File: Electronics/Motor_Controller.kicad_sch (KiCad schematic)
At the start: 1 part, among them U1 RP2040

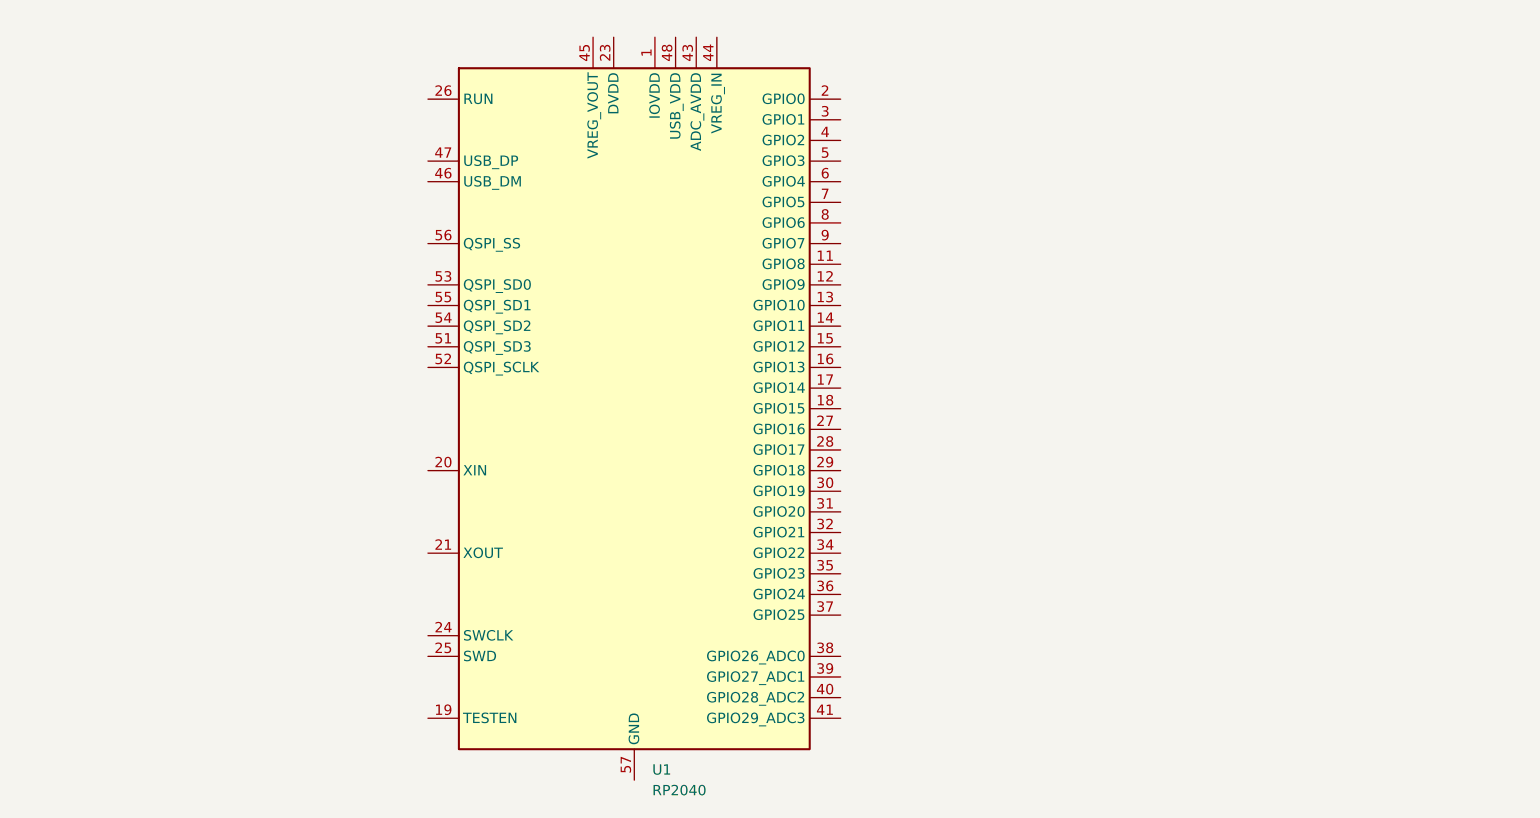
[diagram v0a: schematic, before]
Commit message: components for motor controller
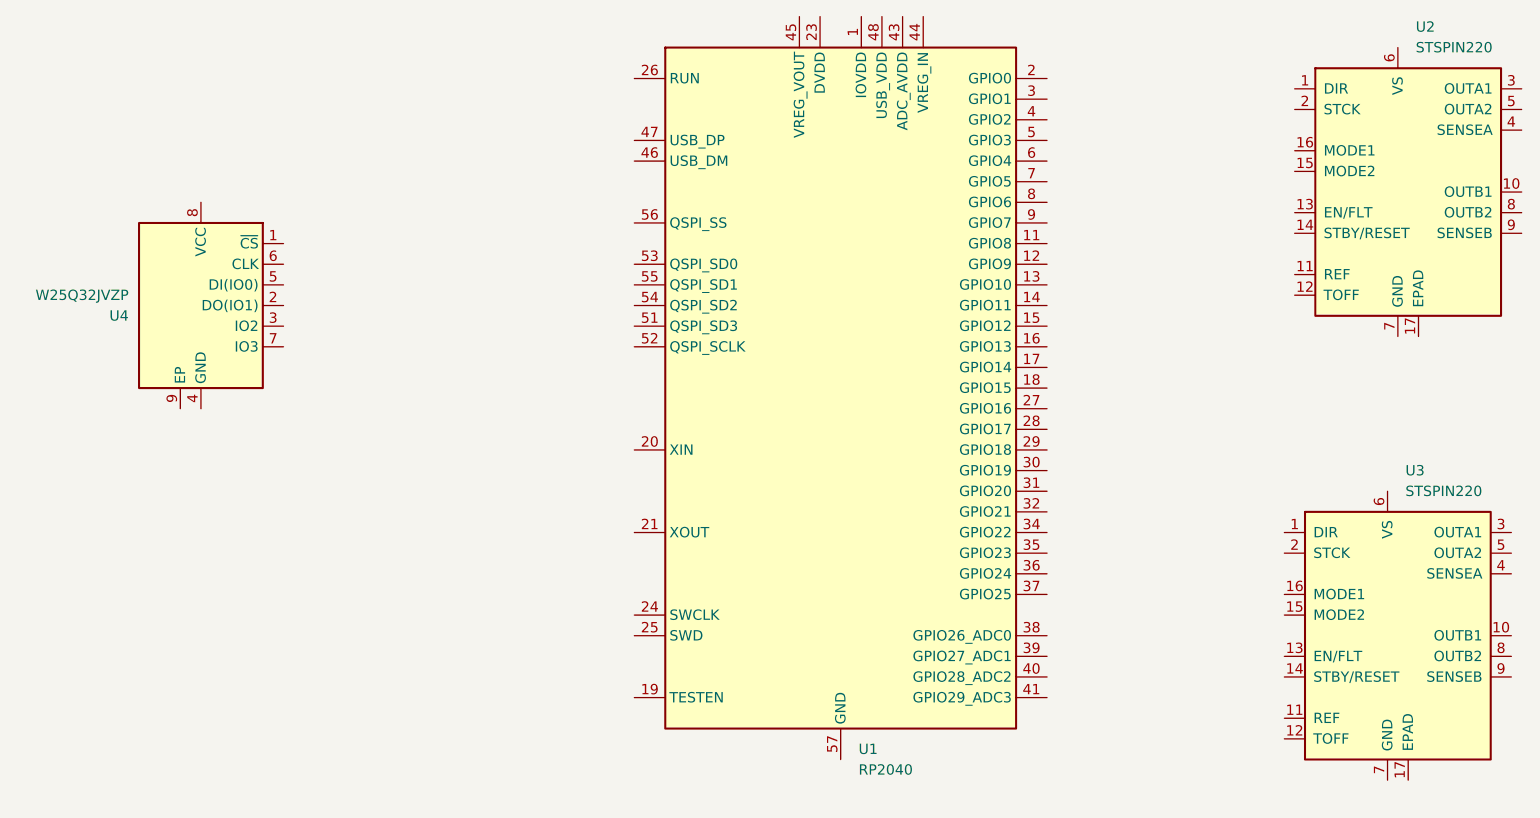
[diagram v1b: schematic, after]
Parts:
- added U2, U3: STSPIN220, Package_DFN_QFN:VQFN-16-1EP_3x3mm_P0.5mm_EP1.8x1.8mm, symbol Driver_Motor:STSPIN220
- added U4: W25Q32JVZP, Package_SON:WSON-8-1EP_6x5mm_P1.27mm_EP3.4x4.3mm, symbol Memory_Flash:W25Q32JVZP
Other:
- moved on the sheet: U1
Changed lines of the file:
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@@
 (kicad_sch (version 20230121) (generator eeschema)
   (paper "A4")
-  (symbol (lib_id "MCU_RaspberryPi:RP2040") (at 91.44 83.82 0) (unit 1)
+  (symbol (lib_id "Driver_Motor:STSPIN220") (at 184.15 111.76 0) (unit 1)
     (in_bom yes) (on_board yes) (dnp no) (fields_autoplaced)
-    (property "Reference" "U1" (at 93.6341 128.27 0)
+    (property "Reference" "U3" (at 186.3441 91.44 0)
       (effects (font (size 1.27 1.27)) (justify left))
     )
-    (property "Value" "RP2040" (at 93.6341 130.81 0)
+    (property "Value" "STSPIN220" (at 186.3441 93.98 0)
       (effects (font (size 1.27 1.27)) (justify left))
     )
-    (property "Footprint" "Package_DFN_QFN:QFN-56-1EP_7x7mm_P0.4mm_EP3.2x3.2mm" (at 91.44 83.82 0)
+    (property "Footprint" "Package_DFN_QFN:VQFN-16-1EP_3x3mm_P0.5mm_EP1.8x1.8mm" (at 189.23 92.71 0)
+      (effects (font (size 1.27 1.27)) (justify left) hide)
+    )
+    (property "Datasheet" "www.st.com/resource/en/datasheet/stspin220.pdf" (at 187.96 105.41 0)
       (effects (font (size 1.27 1.27)) hide)
     )
-    (property "Datasheet" "https://datasheets.raspberrypi.com/rp2040/rp2040-datasheet.pdf" (at 91.44 83.82 0)
+    (pin "5")
+    (pin "6")
+    (pin "13")
+    (pin "11")
+    (pin "14")
+    (pin "12")
+    (pin "15")
+    (pin "10")
+    (pin "16")
+    (pin "9")
+    (pin "1")
+    (pin "7")
+    (pin "3")
+    (pin "2")
+    (pin "8")
+    (pin "4")
+    (pin "17")
+    (instances
+      (project "Electronics"
+        (path "/4c70cac4-2e87-4919-a1c8-fe5f41acf493/95aef9fc-3811-4af8-99a5-cda59dbef7fc"
+          (reference "U3") (unit 1)
+        )
+      )
+    )
+  )
+  (symbol (lib_id "MCU_RaspberryPi:RP2040") (at 116.84 81.28 0) (unit 1)
+    (in_bom yes) (on_board yes) (dnp no) (fields_autoplaced)
+    (property "Reference" "U1" (at 119.0341 125.73 0)
+      (effects (font (size 1.27 1.27)) (justify left))
+    )
+    (property "Value" "RP2040" (at 119.0341 128.27 0)
+      (effects (font (size 1.27 1.27)) (justify left))
+    )
+    (property "Footprint" "Package_DFN_QFN:QFN-56-1EP_7x7mm_P0.4mm_EP3.2x3.2mm" (at 116.84 81.28 0)
+      (effects (font (size 1.27 1.27)) hide)
+    )
+    (property "Datasheet" "https://datasheets.raspberrypi.com/rp2040/rp2040-datasheet.pdf" (at 116.84 81.28 0)
       (effects (font (size 1.27 1.27)) hide)
     )
@@
         )
       )
+    )
+  )
+  (symbol (lib_id "Driver_Motor:STSPIN220") (at 185.42 57.15 0) (unit 1)
+    (in_bom yes) (on_board yes) (dnp no) (fields_autoplaced)
+    (property "Reference" "U2" (at 187.6141 36.83 0)
+      (effects (font (size 1.27 1.27)) (justify left))
+    )
+    (property "Value" "STSPIN220" (at 187.6141 39.37 0)
+      (effects (font (size 1.27 1.27)) (justify left))
+    )
+    (property "Footprint" "Package_DFN_QFN:VQFN-16-1EP_3x3mm_P0.5mm_EP1.8x1.8mm" (at 190.5 38.1 0)
+      (effects (font (size 1.27 1.27)) (justify left) hide)
+    )
+    (property "Datasheet" "www.st.com/resource/en/datasheet/stspin220.pdf" (at 189.23 50.8 0)
+      (effects (font (size 1.27 1.27)) hide)
+    )
+    (pin "5")
+    (pin "6")
+    (pin "13")
+    (pin "11")
+    (pin "14")
+    (pin "12")
+    (pin "15")
+    (pin "10")
+    (pin "16")
+    (pin "9")
+    (pin "1")
+    (pin "7")
+    (pin "3")
+    (pin "2")
+    (pin "8")
+    (pin "4")
+    (pin "17")
+    (instances
+      (project "Electronics"
+        (path "/4c70cac4-2e87-4919-a1c8-fe5f41acf493/95aef9fc-3811-4af8-99a5-cda59dbef7fc"
+          (reference "U2") (unit 1)
+        )
+      )
+    )
+  )
+  (symbol (lib_id "Memory_Flash:W25Q32JVZP") (at 38.1 71.12 0) (mirror y) (unit 1)
+    (in_bom yes) (on_board yes) (dnp no)
+    (property "Reference" "U4" (at 29.21 72.39 0)
+      (effects (font (size 1.27 1.27)) (justify left))
+    )
+    (property "Value" "W25Q32JVZP" (at 29.21 69.85 0)
+      (effects (font (size 1.27 1.27)) (justify left))
+    )
+    (property "Footprint" "Package_SON:WSON-8-1EP_6x5mm_P1.27mm_EP3.4x4.3mm" (at 38.1 71.12 0)
+      (effects (font (size 1.27 1.27)) hide)
+    )
+    (property "Datasheet" "http://www.winbond.com/resource-files/w25q32jv%20revg%2003272018%20plus.pdf" (at 38.1 73.66 0)
+      (effects (font (size 1.27 1.27)) hide)
+    )
+    (pin "9")
+    (pin "8")
+    (pin "3")
+    (pin "1")
+    (pin "6")
+    (pin "2")
+    (pin "7")
+    (pin "4")
+    (pin "5")
+    (instances
+      (project "Electronics"
+        (path "/4c70cac4-2e87-4919-a1c8-fe5f41acf493/95aef9fc-3811-4af8-99a5-cda59dbef7fc"
+          (reference "U4") (unit 1)
+        )
+      )

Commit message: symbol library
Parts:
- removed U2, U3: STSPIN220, Package_DFN_QFN:VQFN-16-1EP_3x3mm_P0.5mm_EP1.8x1.8mm, symbol Driver_Motor:STSPIN220
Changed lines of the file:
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@@
 (kicad_sch (version 20230121) (generator eeschema)
   (paper "A4")
-  (symbol (lib_id "Driver_Motor:STSPIN220") (at 184.15 111.76 0) (unit 1)
-    (in_bom yes) (on_board yes) (dnp no) (fields_autoplaced)
-    (property "Reference" "U3" (at 186.3441 91.44 0)
-      (effects (font (size 1.27 1.27)) (justify left))
-    )
-    (property "Value" "STSPIN220" (at 186.3441 93.98 0)
-      (effects (font (size 1.27 1.27)) (justify left))
-    )
-    (property "Footprint" "Package_DFN_QFN:VQFN-16-1EP_3x3mm_P0.5mm_EP1.8x1.8mm" (at 189.23 92.71 0)
-      (effects (font (size 1.27 1.27)) (justify left) hide)
-    )
-    (property "Datasheet" "www.st.com/resource/en/datasheet/stspin220.pdf" (at 187.96 105.41 0)
-      (effects (font (size 1.27 1.27)) hide)
-    )
-    (pin "5")
-    (pin "6")
-    (pin "13")
-    (pin "11")
-    (pin "14")
-    (pin "12")
-    (pin "15")
-    (pin "10")
-    (pin "16")
-    (pin "9")
-    (pin "1")
-    (pin "7")
-    (pin "3")
-    (pin "2")
-    (pin "8")
-    (pin "4")
-    (pin "17")
-    (instances
-      (project "Electronics"
-        (path "/4c70cac4-2e87-4919-a1c8-fe5f41acf493/95aef9fc-3811-4af8-99a5-cda59dbef7fc"
-          (reference "U3") (unit 1)
-        )
-      )
-    )
-  )
   (symbol (lib_id "MCU_RaspberryPi:RP2040") (at 116.84 81.28 0) (unit 1)
     (in_bom yes) (on_board yes) (dnp no) (fields_autoplaced)
@@
         )
       )
-    )
-  )
-  (symbol (lib_id "Driver_Motor:STSPIN220") (at 185.42 57.15 0) (unit 1)
-    (in_bom yes) (on_board yes) (dnp no) (fields_autoplaced)
-    (property "Reference" "U2" (at 187.6141 36.83 0)
-      (effects (font (size 1.27 1.27)) (justify left))
-    )
-    (property "Value" "STSPIN220" (at 187.6141 39.37 0)
-      (effects (font (size 1.27 1.27)) (justify left))
-    )
-    (property "Footprint" "Package_DFN_QFN:VQFN-16-1EP_3x3mm_P0.5mm_EP1.8x1.8mm" (at 190.5 38.1 0)
-      (effects (font (size 1.27 1.27)) (justify left) hide)
-    )
-    (property "Datasheet" "www.st.com/resource/en/datasheet/stspin220.pdf" (at 189.23 50.8 0)
-      (effects (font (size 1.27 1.27)) hide)
-    )
-    (pin "5")
-    (pin "6")
-    (pin "13")
-    (pin "11")
-    (pin "14")
-    (pin "12")
-    (pin "15")
-    (pin "10")
-    (pin "16")
-    (pin "9")
-    (pin "1")
-    (pin "7")
-    (pin "3")
-    (pin "2")
-    (pin "8")
-    (pin "4")
-    (pin "17")
-    (instances
-      (project "Electronics"
-        (path "/4c70cac4-2e87-4919-a1c8-fe5f41acf493/95aef9fc-3811-4af8-99a5-cda59dbef7fc"
-          (reference "U2") (unit 1)
-        )
-      )

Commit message: TMC2209 FOOTPRINT + SCHEMATIC
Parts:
- added C1: 100nF, symbol Device:C
- added U2: ~, Package_DFN_QFN:QFN-28-1EP_5x5mm_P0.5mm_EP3.75x3.75mm, symbol TMC2209-LA-T:TMC2209-LA-T
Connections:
- new net: C1.2, U2.6 (VCP)
- new net GND: U2.18 (GND), U2.3 (GND)
- new net VBAT: C1.1, U2.22 (VS), U2.28 (VS)
- new net VCC: U2.15 (VCC_IO), U2.17 (VREF)
- no-connect marks 0 -> 1
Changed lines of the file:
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@@
 (kicad_sch (version 20230121) (generator eeschema)
   (paper "A4")
+  (junction (at 194.31 27.94) (diameter 0) (color 0 0 0 0)
+  )
+  (junction (at 194.31 34.29) (diameter 0) (color 0 0 0 0)
+  )
+  (junction (at 195.58 86.36) (diameter 0) (color 0 0 0 0)
+  )
+  (no_connect (at 200.66 35.56))
+  (wire (pts (xy 194.31 34.29) (xy 195.58 34.29))
+    (stroke (width 0) (type default))
+  )
+  (wire (pts (xy 194.31 25.4) (xy 194.31 27.94))
+    (stroke (width 0) (type default))
+  )
+  (wire (pts (xy 173.99 27.94) (xy 194.31 27.94))
+    (stroke (width 0) (type default))
+  )
+  (wire (pts (xy 195.58 34.29) (xy 195.58 35.56))
+    (stroke (width 0) (type default))
+  )
+  (wire (pts (xy 173.99 30.48) (xy 173.99 27.94))
+    (stroke (width 0) (type default))
+  )
+  (wire (pts (xy 194.31 85.09) (xy 194.31 86.36))
+    (stroke (width 0) (type default))
+  )
+  (wire (pts (xy 176.53 41.91) (xy 173.99 41.91))
+    (stroke (width 0) (type default))
+  )
+  (wire (pts (xy 194.31 34.29) (xy 193.04 34.29))
+    (stroke (width 0) (type default))
+  )
+  (wire (pts (xy 173.99 41.91) (xy 173.99 38.1))
+    (stroke (width 0) (type default))
+  )
+  (wire (pts (xy 193.04 34.29) (xy 193.04 35.56))
+    (stroke (width 0) (type default))
+  )
+  (wire (pts (xy 194.31 27.94) (xy 194.31 34.29))
+    (stroke (width 0) (type default))
+  )
+  (wire (pts (xy 194.31 86.36) (xy 195.58 86.36))
+    (stroke (width 0) (type default))
+  )
+  (wire (pts (xy 195.58 86.36) (xy 196.85 86.36))
+    (stroke (width 0) (type default))
+  )
+  (wire (pts (xy 195.58 86.36) (xy 195.58 87.63))
+    (stroke (width 0) (type default))
+  )
+  (wire (pts (xy 196.85 85.09) (xy 196.85 86.36))
+    (stroke (width 0) (type default))
+  )
+  (hierarchical_label "VBAT" (shape input) (at 194.31 25.4 90) (fields_autoplaced)
+    (effects (font (size 1.27 1.27)) (justify left))
+  )
+  (symbol (lib_id "TMC2209-LA-T:TMC2209-LA-T") (at 195.58 60.96 0) (unit 1)
+    (in_bom yes) (on_board yes) (dnp no) (fields_autoplaced)
+    (property "Reference" "U2" (at 199.0441 87.63 0)
+      (effects (font (size 1.27 1.27)) (justify left))
+    )
+    (property "Value" "~" (at 186.69 106.68 0)
+      (effects (font (size 1.27 1.27)))
+    )
+    (property "Footprint" "Package_DFN_QFN:QFN-28-1EP_5x5mm_P0.5mm_EP3.75x3.75mm" (at 186.69 106.68 0)
+      (effects (font (size 1.27 1.27)) hide)
+    )
+    (property "Datasheet" "https://www.digikey.com/en/products/detail/analog-devices-inc-maxim-integrated/TMC2209-LA-T/10232491" (at 186.69 106.68 0)
+      (effects (font (size 1.27 1.27)) hide)
+    )
+    (pin "24")
+    (pin "18")
+    (pin "2")
+    (pin "9")
+    (pin "17")
+    (pin "6")
+    (pin "15")
+    (pin "14")
+    (pin "16")
+    (pin "13")
+    (pin "1")
+    (pin "23")
+    (pin "28")
+    (pin "4")
+    (pin "8")
+    (pin "12")
+    (pin "20")
+    (pin "22")
+    (pin "27")
+    (pin "21")
+    (pin "3")
+    (pin "26")
+    (pin "5")
+    (pin "10")
+    (pin "7")
+    (pin "11")
+    (pin "19")
+    (instances
+      (project "Electronics"
+        (path "/4c70cac4-2e87-4919-a1c8-fe5f41acf493/95aef9fc-3811-4af8-99a5-cda59dbef7fc"
+          (reference "U2") (unit 1)
+        )
+      )
+    )
+  )
+  (symbol (lib_id "power:VCC") (at 190.5 35.56 0) (unit 1)
+    (in_bom yes) (on_board yes) (dnp no)
+    (property "Reference" "#PWR06" (at 190.5 39.37 0)
+      (effects (font (size 1.27 1.27)) hide)
+    )
+    (property "Value" "VCC" (at 190.5 31.75 0)
+      (effects (font (size 1.27 1.27)))
+    )
+    (property "Footprint" "" (at 190.5 35.56 0)
+      (effects (font (size 1.27 1.27)) hide)
+    )
+    (property "Datasheet" "" (at 190.5 35.56 0)
+      (effects (font (size 1.27 1.27)) hide)
+    )
+    (pin "1")
+    (instances
+      (project "Electronics"
+        (path "/4c70cac4-2e87-4919-a1c8-fe5f41acf493/95aef9fc-3811-4af8-99a5-cda59dbef7fc"
+          (reference "#PWR06") (unit 1)
+        )
+      )
+    )
+  )
   (symbol (lib_id "MCU_RaspberryPi:RP2040") (at 116.84 81.28 0) (unit 1)
     (in_bom yes) (on_board yes) (dnp no) (fields_autoplaced)
@@
         )
       )
+    )
+  )
+  (symbol (lib_id "power:VCC") (at 198.12 35.56 0) (unit 1)
+    (in_bom yes) (on_board yes) (dnp no)
+    (property "Reference" "#PWR07" (at 198.12 39.37 0)
+      (effects (font (size 1.27 1.27)) hide)
+    )
+    (property "Value" "VCC" (at 198.12 31.75 0)
+      (effects (font (size 1.27 1.27)))
+    )
+    (property "Footprint" "" (at 198.12 35.56 0)
+      (effects (font (size 1.27 1.27)) hide)
+    )
+    (property "Datasheet" "" (at 198.12 35.56 0)
+      (effects (font (size 1.27 1.27)) hide)
+    )
+    (pin "1")
+    (instances
+      (project "Electronics"
+        (path "/4c70cac4-2e87-4919-a1c8-fe5f41acf493/95aef9fc-3811-4af8-99a5-cda59dbef7fc"
+          (reference "#PWR07") (unit 1)
+        )
+      )
+    )
+  )
+  (symbol (lib_id "Device:C") (at 173.99 34.29 0) (unit 1)
+    (in_bom yes) (on_board yes) (dnp no)
+    (property "Reference" "C1" (at 177.8 33.02 0)
+      (effects (font (size 1.27 1.27)) (justify left))
+    )
+    (property "Value" "100nF" (at 177.8 35.56 0)
+      (effects (font (size 1.27 1.27)) (justify left))
+    )
+    (property "Footprint" "" (at 174.9552 38.1 0)
+      (effects (font (size 1.27 1.27)) hide)
+    )
+    (property "Datasheet" "~" (at 173.99 34.29 0)
+      (effects (font (size 1.27 1.27)) hide)
+    )
+    (pin "2")
+    (pin "1")
+    (instances
+      (project "Electronics"
+        (path "/4c70cac4-2e87-4919-a1c8-fe5f41acf493/95aef9fc-3811-4af8-99a5-cda59dbef7fc"
+          (reference "C1") (unit 1)
+        )
+      )
+    )
+  )
+  (symbol (lib_id "power:GND") (at 195.58 87.63 0) (unit 1)
+    (in_bom yes) (on_board yes) (dnp no) (fields_autoplaced)
+    (property "Reference" "#PWR08" (at 195.58 93.98 0)
+      (effects (font (size 1.27 1.27)) hide)
+    )
+    (property "Value" "GND" (at 195.58 92.71 0)
+      (effects (font (size 1.27 1.27)))
+    )
+    (property "Footprint" "" (at 195.58 87.63 0)
+      (effects (font (size 1.27 1.27)) hide)
+    )
+    (property "Datasheet" "" (at 195.58 87.63 0)
+      (effects (font (size 1.27 1.27)) hide)
+    )
+    (pin "1")
+    (instances
+      (project "Electronics"
+        (path "/4c70cac4-2e87-4919-a1c8-fe5f41acf493/95aef9fc-3811-4af8-99a5-cda59dbef7fc"
+          (reference "#PWR08") (unit 1)
+        )
+      )
